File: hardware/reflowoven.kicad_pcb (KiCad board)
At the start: 2 copper layers, 63.5 x 67.3 mm, 40 parts, among them P1 USB-A-SHLD, P2 CONN_6, P3 CONN_2, P4 CONN_2, P5 CONN_01X08, U1 MSP430G2553IPW20, U2 FT232RL, U3 LM317, U4 ULN2003A, U5 MCHRM3H, U6 MCHRM3H, U7 MCHRM3H, U8 MCHRM3H, X1 CRYSTAL

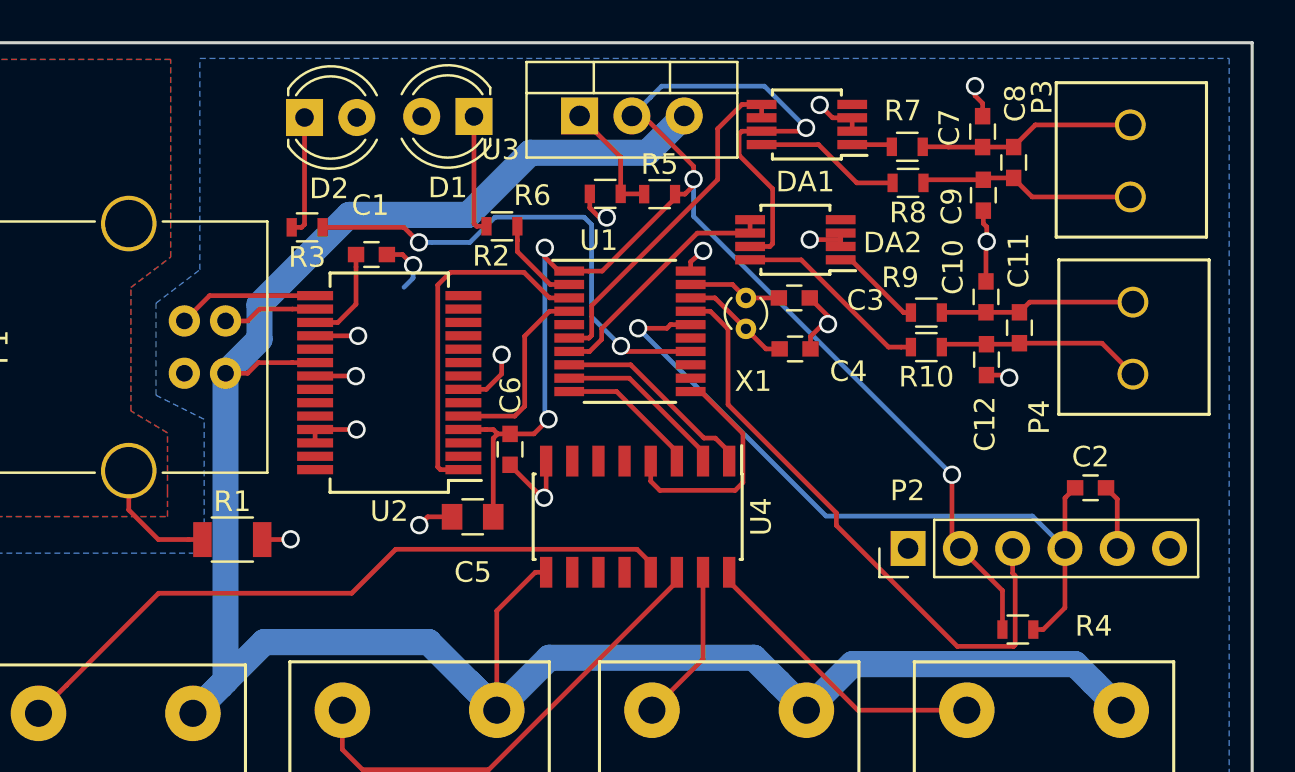
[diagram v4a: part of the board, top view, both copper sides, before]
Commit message: Update schematic and PCB to include additional 1M ohm resitor on thermocouple - term.  This seems to stablize the temp readings.
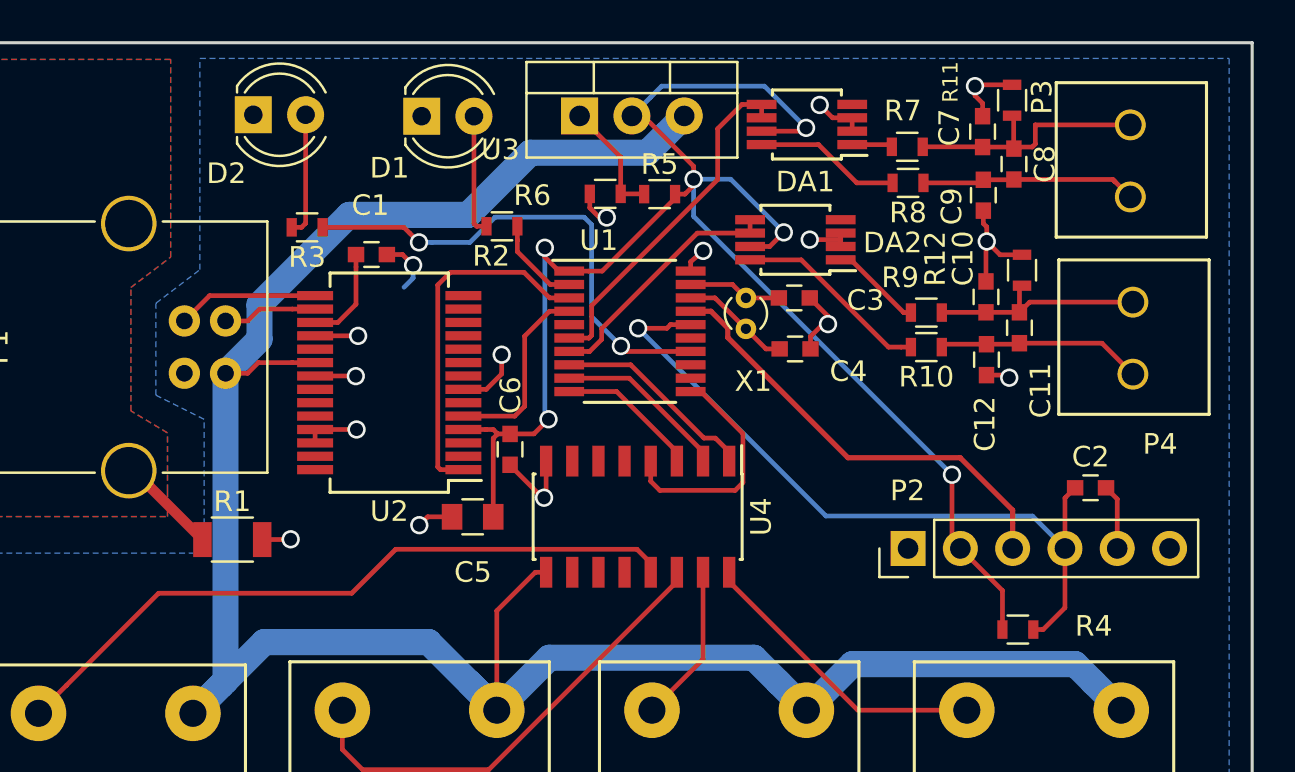
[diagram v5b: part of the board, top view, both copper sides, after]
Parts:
- added R11: 1M, Resistors_SMD:R_0603, F.Cu at (180.1, 150.1)
- added R12: 1M, Resistors_SMD:R_0603, F.Cu at (180.6, 158.4)
- moved D1 2.54 mm to (151.4, 150.9), turned to 0 degrees
- moved D2 2.49 mm to (143.3, 150.8)
- moved C8 0.08 mm to (180.2, 153.2)
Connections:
- net +3V3 renamed +3.3V
- D1 pad 1: Net-(D1-Pad1) -> GND
- D1 pad 2: GND -> Net-(D1-Pad2)
- D2 pad 1: Net-(D2-Pad1) -> GND
- D2 pad 2: GND -> Net-(D2-Pad2)
- R2 pad 2: Net-(D1-Pad1) -> Net-(D1-Pad2)
- R3 pad 2: Net-(D2-Pad1) -> Net-(D2-Pad2)
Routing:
- net /TCK: track 29.8 -> 21.8 mm
- net Net-(D2-Pad2): track 0.00 -> 6.03 mm
- net Net-(D1-Pad2): track 0.00 -> 5.88 mm
- net Net-(D2-Pad1): track 5.87 -> 0.00 mm
- net Net-(D1-Pad1): track 5.87 -> 0.00 mm
- net GND: track 40.9 -> 44.7 mm
- net /Relays and Themocouples/Thermocouple_1-: track 10.5 -> 12.7 mm
- net /Relays and Themocouples/Thermocouple_2-: track 9.49 -> 10.8 mm
- net /ESD_RING: track 6.09 -> 4.97 mm
- net +3.3V: track 80.6 -> 79.6 mm, vias 5 -> 6

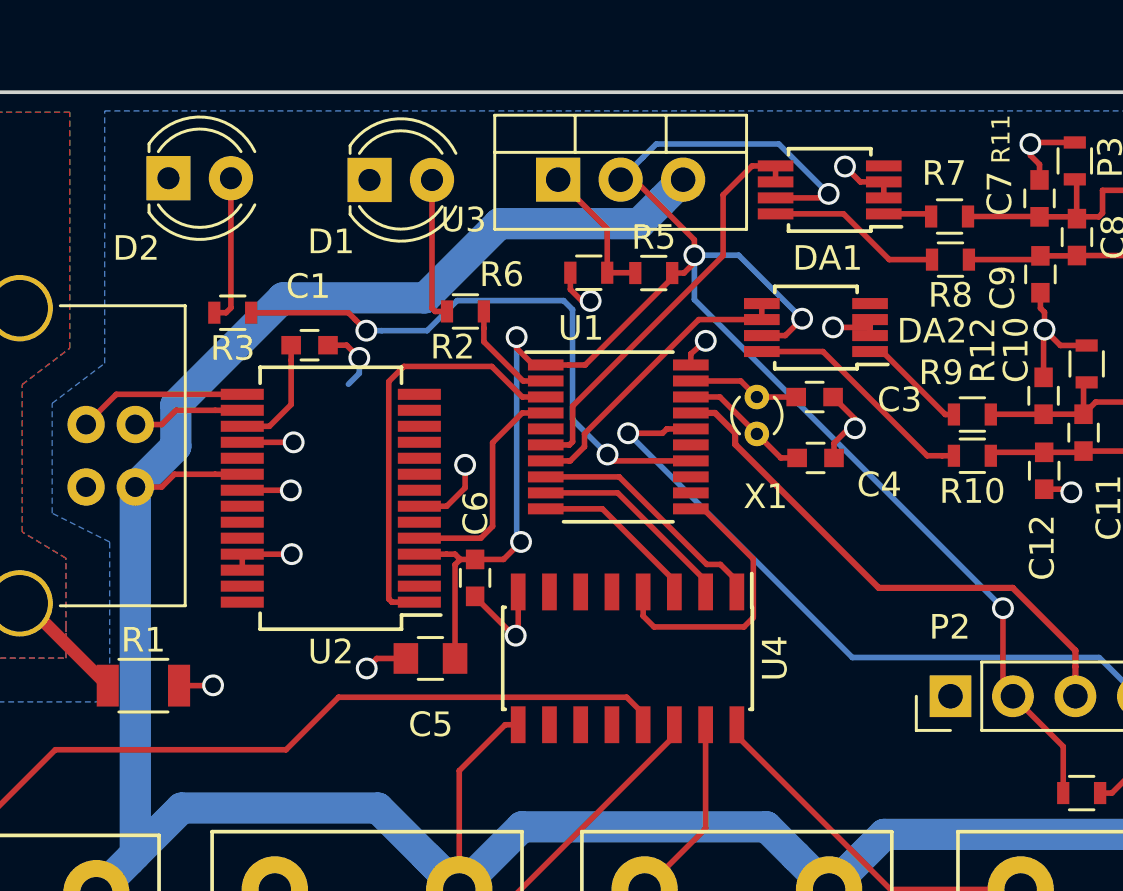
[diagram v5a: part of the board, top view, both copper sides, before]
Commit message: Updated schematic and PCB to 100% match footprints
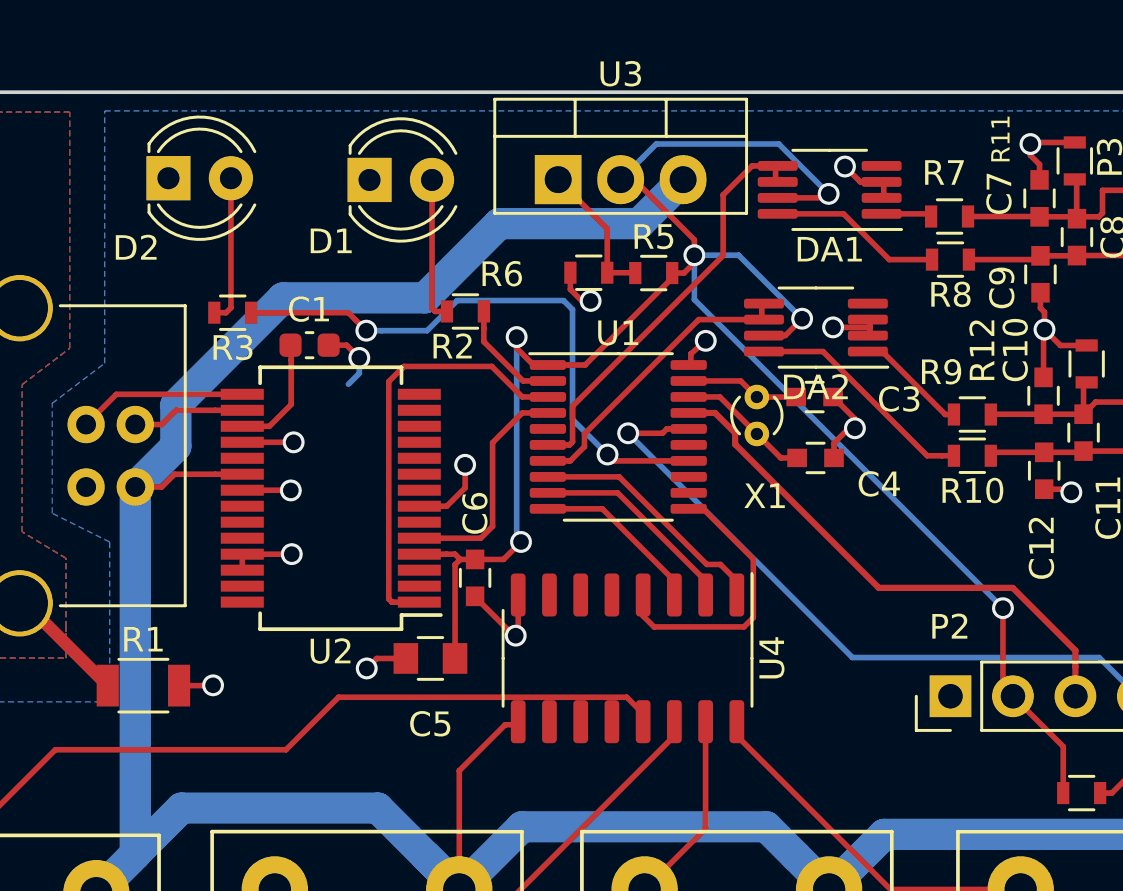
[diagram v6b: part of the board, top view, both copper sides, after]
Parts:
- C1: footprint Capacitors_SMD:C_0603 -> Capacitor_SMD:C_0603_1608Metric
- DA1, DA2: footprint Housings_SSOP:MSOP-8_3x3mm_Pitch0.65mm -> Package_SO:MSOP-8_3x3mm_P0.65mm
- U1: footprint Housings_SSOP:TSSOP-20_4.4x6.5mm_Pitch0.65mm -> Package_SO:TSSOP-20_4.4x6.5mm_P0.65mm
- U2: footprint Housings_SSOP:SSOP-28_5.3x10.2mm_Pitch0.65mm -> Package_SO:SSOP-28_5.3x10.2mm_P0.65mm
- U3: footprint TO_SOT_Packages_THT:TO-220_Vertical -> Package_TO_SOT_THT:TO-220-3_Vertical
- U4: footprint Housings_SOIC:SOIC-16_3.9x9.9mm_Pitch1.27mm -> Package_SO:SO-16_3.9x9.9mm_P1.27mm
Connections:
- net +3.3V renamed +3V3
- C1 pad 1: Net-(C1-Pad1) -> GND
- C1 pad 2: GND -> Net-(C1-Pad2)
- DA1 pad 4: Net-(DA1-Pad4) -> unconnected-(DA1-Pad4)
- DA2 pad 4: Net-(DA2-Pad4) -> unconnected-(DA2-Pad4)
- P1 pad 2: /USB_DM -> /USB_DP
- P1 pad 3: /USB_DP -> /USB_DM
- P2 pad 1: Net-(P2-Pad1) -> unconnected-(P2-Pad1)
- P2 pad 6: Net-(P2-Pad6) -> unconnected-(P2-Pad6)
- U1 pad 12: Net-(U1-Pad12) -> unconnected-(U1-Pad12)
- U1 pad 13: Net-(U1-Pad13) -> unconnected-(U1-Pad13)
- U1 pad 15: Net-(U1-Pad15) -> unconnected-(U1-Pad15)
- U1 pad 5: Net-(U1-Pad5) -> unconnected-(U1-Pad5)
- U1 pad 6: /TEMP_1 -> unconnected-(U1-Pad6)
- U1 pad 7: /TEMP_2 -> unconnected-(U1-Pad7)
- U2 pad 10: Net-(U2-Pad10) -> unconnected-(U2-Pad10)
- U2 pad 11: Net-(U2-Pad11) -> unconnected-(U2-Pad11)
- U2 pad 12: Net-(U2-Pad12) -> unconnected-(U2-Pad12)
- U2 pad 13: Net-(U2-Pad13) -> unconnected-(U2-Pad13)
- U2 pad 14: Net-(U2-Pad14) -> unconnected-(U2-Pad14)
- U2 pad 15: /USB_DP -> /USB_DM
- U2 pad 16: /USB_DM -> /USB_DP
- U2 pad 17: Net-(C1-Pad1) -> Net-(C1-Pad2)
- U2 pad 19: Net-(U2-Pad19) -> unconnected-(U2-Pad19)
- U2 pad 2: Net-(U2-Pad2) -> unconnected-(U2-Pad2)
- U2 pad 22: Net-(U2-Pad22) -> unconnected-(U2-Pad22)
- U2 pad 23: Net-(U2-Pad23) -> unconnected-(U2-Pad23)
- U2 pad 26: GND -> unconnected-(U2-Pad26)
- U2 pad 27: Net-(U2-Pad27) -> unconnected-(U2-Pad27)
- U2 pad 28: Net-(U2-Pad28) -> unconnected-(U2-Pad28)
- U2 pad 3: Net-(U2-Pad3) -> unconnected-(U2-Pad3)
- U2 pad 6: Net-(U2-Pad6) -> unconnected-(U2-Pad6)
- U2 pad 9: Net-(U2-Pad9) -> unconnected-(U2-Pad9)
- U4 pad 10: Net-(U4-Pad10) -> unconnected-(U4-Pad10)
- U4 pad 11: Net-(U4-Pad11) -> unconnected-(U4-Pad11)
- U4 pad 12: Net-(U4-Pad12) -> unconnected-(U4-Pad12)
- U4 pad 5: Net-(U4-Pad5) -> unconnected-(U4-Pad5)
- U4 pad 6: Net-(U4-Pad6) -> unconnected-(U4-Pad6)
- U4 pad 7: Net-(U4-Pad7) -> unconnected-(U4-Pad7)
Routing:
- net Net-(C1-Pad2): track 0.00 -> 7.51 mm, vias 0 -> 1
- net Net-(C1-Pad1): track 4.77 -> 0.00 mm
- net GND: track 44.7 -> 42.0 mm, vias 16 -> 15
- net /USB_DP: track 6.86 -> 4.59 mm
- net /USB_DM: track 4.59 -> 6.86 mm
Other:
- net class Default removed
